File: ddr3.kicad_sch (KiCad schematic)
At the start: 65 parts, among them U7 AS4C256M16D3, U8 TPS51200DRCT

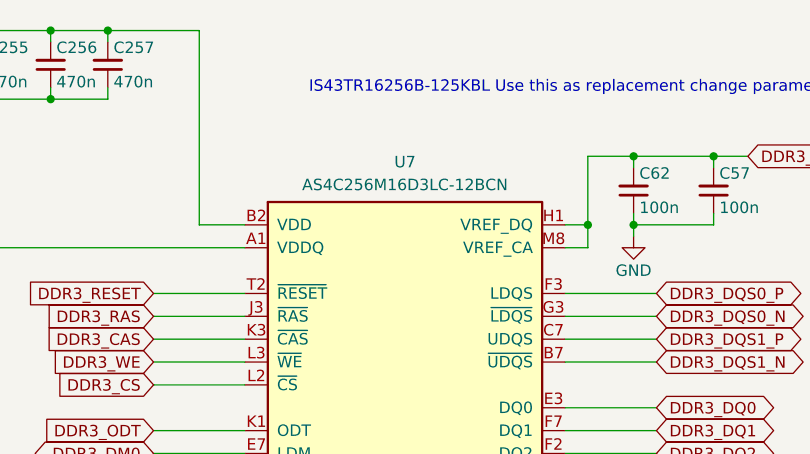
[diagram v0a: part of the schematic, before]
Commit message: ddr3 routing finished
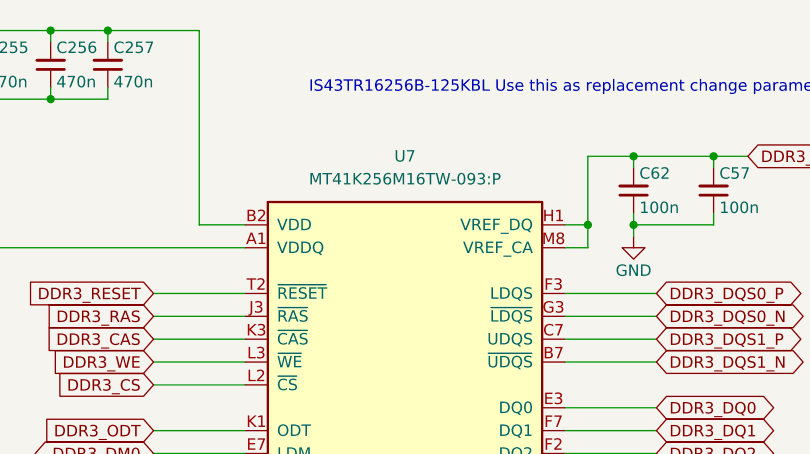
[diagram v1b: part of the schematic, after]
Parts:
- U7: value AS4C256M16D3 -> MT41K256M16TW-093:P; footprint antmicro-footprints:BGA-96-48_7.5x13.5mm_Layout9x16_P0.8mm -> artix-dc-scm:BGA96C80P9X16_800X1400X120; MPN AS4C256M16D3LC-12BCN -> MT41K256M16TW-093:P; Manufacturer Alliance Memory -> Micron
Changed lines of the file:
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@@
 		(fields_autoplaced yes)
 		(property "Reference" "U7"
-			(at 218.44 52.705 0)
+			(at 218.44 52.07 0)
 			(show_name no)
 			(do_not_autoplace no)
@@
 			)
 		)
-		(property "Value" "AS4C256M16D3"
+		(property "Value" "MT41K256M16TW-093:P"
 			(at 251.46 62.23 0)
 			(hide yes)
@@
 			)
 		)
-		(property "Footprint" "antmicro-footprints:BGA-96-48_7.5x13.5mm_Layout9x16_P0.8mm"
+		(property "Footprint" "artix-dc-scm:BGA96C80P9X16_800X1400X120"
 			(at 251.46 64.77 0)
 			(hide yes)
@@
 			)
 		)
-		(property "Datasheet" "https://www.alliancememory.com/wp-content/uploads/AllianceMemory_4G_DDR3L_AS4C256M16D3LC_March2020_Rev1.0.pdf"
+		(property "Datasheet" "https://www.mouser.com/catalog/specsheets/Micron_07-31-2025_MT41K.pdf"
 			(at 251.46 67.31 0)
 			(hide yes)
@@
 			)
 		)
-		(property "Description" "SDRAM - DDR3 Memory IC 4Gbit Parallel 800 MHz 20 ns 96-FBGA (9x13)"
+		(property "Description" "DRAM DDR3 4Gbit 16 96/144TFBGA 1 CT"
 			(at 200.66 59.69 0)
 			(hide yes)
@@
 			)
 		)
-		(property "Manufacturer" "Alliance Memory"
+		(property "Manufacturer" "Micron"
 			(at 251.46 69.85 0)
 			(hide yes)
@@
 			)
 		)
-		(property "MPN" "AS4C256M16D3LC-12BCN"
-			(at 218.44 55.245 0)
+		(property "MPN" "MT41K256M16TW-093:P"
+			(at 218.44 54.61 0)
 			(show_name no)
 			(do_not_autoplace no)

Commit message: a lot of routing and almost all caps of the fpga are placed down
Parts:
- C1, C155, C40, C41, C42, C43, C44, C46, C47, C49, C50, C51, C52, C53, C54, C55, C56, C57, C58, C59, C60, C61, C62, C63, C8, C9: footprint antmicro-footprints:C_0402_1005Metric -> Capacitor_SMD:C_0402_1005Metric
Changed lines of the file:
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@@
 			)
 		)
-		(property "Footprint" "antmicro-footprints:C_0402_1005Metric"
+		(property "Footprint" "Capacitor_SMD:C_0402_1005Metric"
 			(at 162.56 24.13 0)
 			(hide yes)
@@
 			)
 		)
-		(property "Footprint" "antmicro-footprints:C_0402_1005Metric"
+		(property "Footprint" "Capacitor_SMD:C_0402_1005Metric"
 			(at 198.12 181.61 0)
 			(hide yes)
@@
 			)
 		)
-		(property "Footprint" "antmicro-footprints:C_0402_1005Metric"
+		(property "Footprint" "Capacitor_SMD:C_0402_1005Metric"
 			(at 168.91 24.13 0)
 			(hide yes)
@@
 			)
 		)
-		(property "Footprint" "antmicro-footprints:C_0402_1005Metric"
+		(property "Footprint" "Capacitor_SMD:C_0402_1005Metric"
 			(at 116.84 24.13 0)
 			(hide yes)
@@
 			)
 		)
-		(property "Footprint" "antmicro-footprints:C_0402_1005Metric"
+		(property "Footprint" "Capacitor_SMD:C_0402_1005Metric"
 			(at 124.46 24.13 0)
 			(hide yes)
@@
 			)
 		)
-		(property "Footprint" "antmicro-footprints:C_0402_1005Metric"
+		(property "Footprint" "Capacitor_SMD:C_0402_1005Metric"
 			(at 132.08 24.13 0)
 			(hide yes)
@@
 			)
 		)
-		(property "Footprint" "antmicro-footprints:C_0402_1005Metric"
+		(property "Footprint" "Capacitor_SMD:C_0402_1005Metric"
 			(at 139.7 24.13 0)
 			(hide yes)
@@
 			)
 		)
-		(property "Footprint" "antmicro-footprints:C_0402_1005Metric"
+		(property "Footprint" "Capacitor_SMD:C_0402_1005Metric"
 			(at 147.32 24.13 0)
 			(hide yes)
@@
 			)
 		)
-		(property "Footprint" "antmicro-footprints:C_0402_1005Metric"
+		(property "Footprint" "Capacitor_SMD:C_0402_1005Metric"
 			(at 154.94 24.13 0)
 			(hide yes)
@@
 			)
 		)
-		(property "Footprint" "antmicro-footprints:C_0402_1005Metric"
+		(property "Footprint" "Capacitor_SMD:C_0402_1005Metric"
 			(at 101.6 190.5 0)
 			(hide yes)
@@
 			)
 		)
-		(property "Footprint" "antmicro-footprints:C_0402_1005Metric"
+		(property "Footprint" "Capacitor_SMD:C_0402_1005Metric"
 			(at 116.84 38.1 0)
 			(hide yes)
@@
 			)
 		)
-		(property "Footprint" "antmicro-footprints:C_0402_1005Metric"
+		(property "Footprint" "Capacitor_SMD:C_0402_1005Metric"
 			(at 124.46 38.1 0)
 			(hide yes)
@@
 			)
 		)
-		(property "Footprint" "antmicro-footprints:C_0402_1005Metric"
+		(property "Footprint" "Capacitor_SMD:C_0402_1005Metric"
 			(at 132.08 38.1 0)
 			(hide yes)
@@
 			)
 		)
-		(property "Footprint" "antmicro-footprints:C_0402_1005Metric"
+		(property "Footprint" "Capacitor_SMD:C_0402_1005Metric"
 			(at 139.7 38.1 0)
 			(hide yes)
@@
 			)
 		)
-		(property "Footprint" "antmicro-footprints:C_0402_1005Metric"
+		(property "Footprint" "Capacitor_SMD:C_0402_1005Metric"
 			(at 147.32 38.1 0)
 			(hide yes)
@@
 			)
 		)
-		(property "Footprint" "antmicro-footprints:C_0402_1005Metric"
+		(property "Footprint" "Capacitor_SMD:C_0402_1005Metric"
 			(at 154.94 38.1 0)
 			(hide yes)
@@
 			)
 		)
-		(property "Footprint" "antmicro-footprints:C_0402_1005Metric"
+		(property "Footprint" "Capacitor_SMD:C_0402_1005Metric"
 			(at 265.43 38.1 0)
 			(hide yes)
@@
 			)
 		)
-		(property "Footprint" "antmicro-footprints:C_0402_1005Metric"
+		(property "Footprint" "Capacitor_SMD:C_0402_1005Metric"
 			(at 256.54 38.1 0)
 			(hide yes)
@@
 			)
 		)
-		(property "Footprint" "antmicro-footprints:C_0402_1005Metric"
+		(property "Footprint" "Capacitor_SMD:C_0402_1005Metric"
 			(at 190.5 181.61 0)
 			(hide yes)
@@
 			)
 		)
-		(property "Footprint" "antmicro-footprints:C_0402_1005Metric"
+		(property "Footprint" "Capacitor_SMD:C_0402_1005Metric"
 			(at 182.88 181.61 0)
 			(hide yes)
@@
 			)
 		)
-		(property "Footprint" "antmicro-footprints:C_0402_1005Metric"
+		(property "Footprint" "Capacitor_SMD:C_0402_1005Metric"
 			(at 149.86 181.61 0)
 			(hide yes)
@@
 			)
 		)
-		(property "Footprint" "antmicro-footprints:C_0402_1005Metric"
+		(property "Footprint" "Capacitor_SMD:C_0402_1005Metric"
 			(at 95.25 171.45 0)
 			(hide yes)
@@
 			)
 		)
-		(property "Footprint" "antmicro-footprints:C_0402_1005Metric"
+		(property "Footprint" "Capacitor_SMD:C_0402_1005Metric"
 			(at 127 208.28 0)
 			(hide yes)
@@
 			)
 		)
-		(property "Footprint" "antmicro-footprints:C_0402_1005Metric"
+		(property "Footprint" "Capacitor_SMD:C_0402_1005Metric"
 			(at 157.48 198.12 0)
 			(hide yes)
@@
 			)
 		)
-		(property "Footprint" "antmicro-footprints:C_0402_1005Metric"
+		(property "Footprint" "Capacitor_SMD:C_0402_1005Metric"
 			(at 149.86 198.12 0)
 			(hide yes)
@@
 			)
 		)
-		(property "Footprint" "antmicro-footprints:C_0402_1005Metric"
+		(property "Footprint" "Capacitor_SMD:C_0402_1005Metric"
 			(at 121.92 139.7 0)
 			(hide yes)

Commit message: a lot of poin swaps
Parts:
- C221, C255, C256, C257, C49, C50, C51, C52, C53, C54, C55, C56, C58, C59, C60, C61, C8, C9: MPN C1005X5R1E474M050BB -> GXT155C80J474KE01D; Manufacturer TDK -> Murata Electronics

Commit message: version 1.0 complete
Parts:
- R113, R57, R58, R59: MPN CR0402-FX-1002GLF -> CR0402AFX-1002GAS
- R13: MPN CR0402-FX-4701GLF -> RC0402FR-7D4K7L; Manufacturer Bourns -> YAGEO

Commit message: "In the process of upgrading the ddr memory"
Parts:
- removed C221, C255, C256, C257, C49, C50, C51, C52, C53, C54, C55, C56, C58, C59, C60, C61, C8, C9: C_470n_0402, Capacitor_SMD:C_0402_1005Metric, symbol antmicroCapacitors0402:C_470n_0402
- removed C48: C_4u7_0402, Capacitor_SMD:C_0402_1005Metric, symbol antmicroCapacitors0402:C_4u7_0402
- removed C57, C62, C63: C_100n_6V3_0402, Capacitor_SMD:C_0402_1005Metric, symbol antmicroCapacitorsmisc:C_100n_6V3_0402
- removed R100, R99: R_51R_0402, antmicro-footprints:R_0402_1005Metric, symbol antmicroResistors0402:R_51R_0402
- removed R13: R_4k7_0402, antmicro-footprints:R_0402_1005Metric, symbol antmicroResistors0402:R_4k7_0402
- removed R60: R_240R_0402, antmicro-footprints:R_0402_1005Metric, symbol antmicroResistors0402:R_240R_0402
- removed U7: MT41K256M16TW-093:P, artix-dc-scm:BGA96C80P9X16_800X1400X120, symbol antmicroMemory:AS4C256M16D3
- R113, R162, R163, R164, R167, R168, R169, R170, R171, R172, R173, R174, R175, R176, R177, R178, R179, R180, R181, R182, R183, R184, R54, R55, R56, R57, R58, R59: footprint antmicro-footprints:R_0402_1005Metric -> Resistor_SMD:R_0402_1005Metric
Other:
- note added: "Redo for 2 chips"
- note removed: "IS43TR16256B-125KBL Use this as replacement change parameters in vivado use low power verison"
